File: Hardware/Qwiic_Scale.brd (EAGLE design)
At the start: 25.4 x 35.6 mm, 68 parts, among them J2 Qwiic Right Angle, J3 PTH, J4 Qwiic Right Angle, J6 Spring Terminal, U1 NAU7802

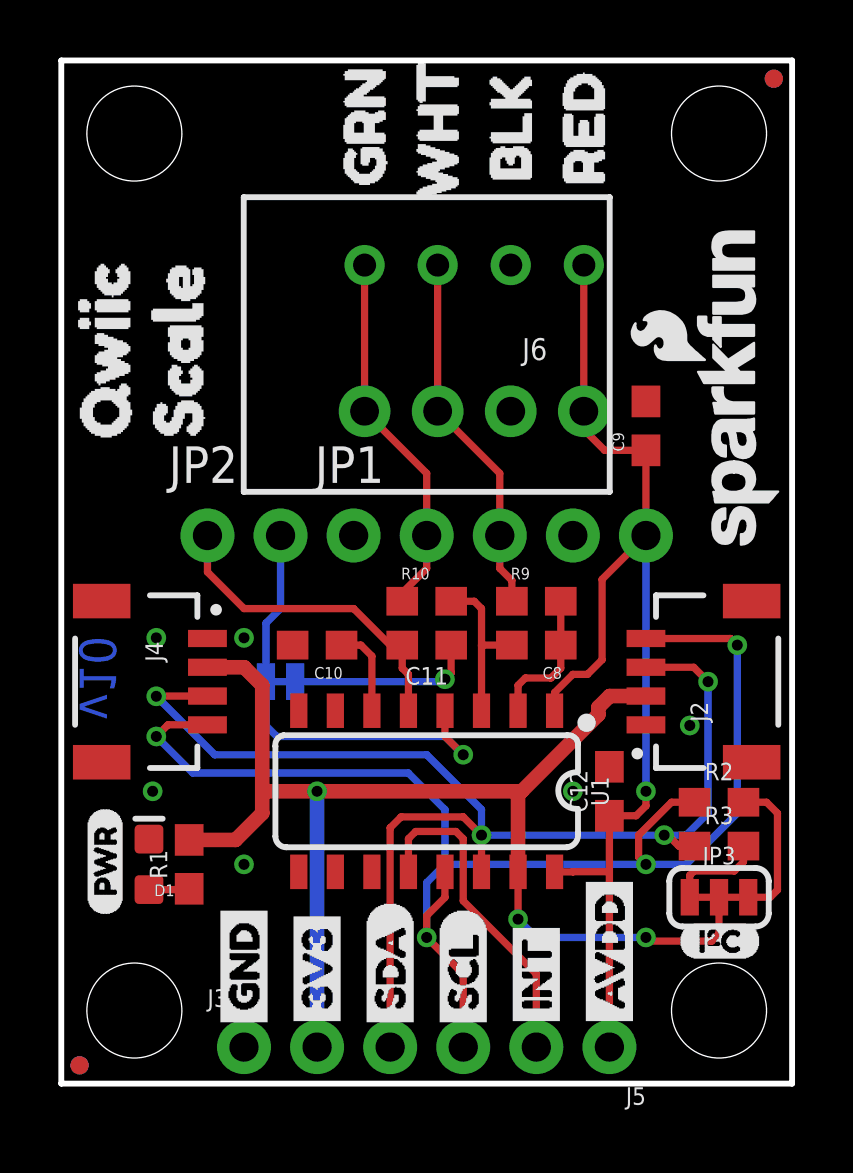
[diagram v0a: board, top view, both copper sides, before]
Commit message: Fixing FP on terminal. Adding ignore.
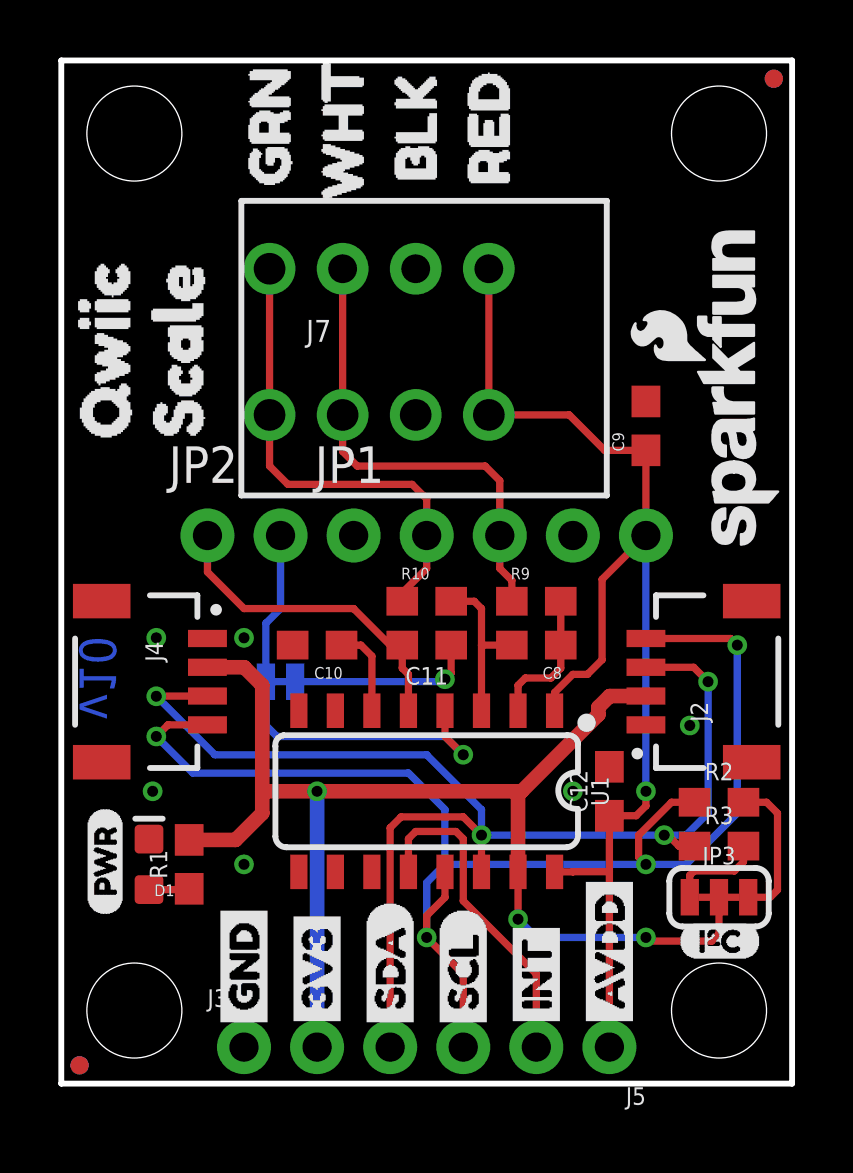
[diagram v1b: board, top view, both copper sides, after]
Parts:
- removed J6: Spring Terminal, SparkFun-Connectors:1X04_SPRING_TERMINAL
- added J7: Spring Terminal, SparkFun-Connectors:1X04_SPRING_TERMINAL
- moved U$41 3.30 mm to (14.9, 30.0)
- moved U$42 3.30 mm to (14.9, 30.4)
- moved U$40 3.30 mm to (7.24, 30.0)
- moved U$37 3.30 mm to (12.3, 29.0)
- moved U$38 3.30 mm to (12.3, 30.1)
- moved U$44 3.30 mm to (9.78, 29.5)
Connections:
- net A+: now also J7.4, J7.8; no longer J6.4, J6.8
- net A-: now also J7.3, J7.7; no longer J6.3, J6.7
- net GND: now also J7.2, J7.6; no longer J6.2, J6.6
- net VDDA: now also J7.1, J7.5; no longer J6.1, J6.5
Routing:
- net A-: track 12.8 -> 16.6 mm
- net A+: track 12.9 -> 16.7 mm
- net VDDA: track 39.6 -> 42.5 mm
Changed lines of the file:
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@@
 <attribute name="VALUE" x="20.32" y="3.302" size="0.6096" layer="27" font="vector" ratio="20" rot="R180"/>
-</element>
-<element name="J6" library="SparkFun-Connectors" package="1X04_SPRING_TERMINAL" value="Spring Terminal" x="18.161" y="25.908" smashed="yes" rot="R180">
-<attribute name="NAME" x="16.891" y="25.908" size="0.762" layer="25" rot="R180"/>
-<attribute name="SF_ID" value="PRT-08075" x="18.161" y="25.908" size="1.778" layer="27" font="vector" ratio="15" rot="R180" display="off"/>
-<attribute name="VALUE" x="16.891" y="27.178" size="0.762" layer="27" rot="R180"/>
 </element>
 <element name="U$12" library="buzzard_labels (62)" package="B#11" value="" x="7.62" y="15.24" smashed="yes" rot="MR90"/>
 <element name="U$13" library="buzzard_labels (62)" package="B#12" value="" x="5.08" y="15.24" smashed="yes" rot="MR90"/>
-<element name="U$37" library="buzzard_labels (64)" package="BLACK5" value="" x="15.621" y="28.956" smashed="yes" rot="MR90"/>
-<element name="U$38" library="buzzard_labels (64)" package="BLK1" value="" x="15.621" y="30.099" smashed="yes" rot="R90"/>
+<element name="U$37" library="buzzard_labels (64)" package="BLACK5" value="" x="12.319" y="28.956" smashed="yes" rot="MR90"/>
+<element name="U$38" library="buzzard_labels (64)" package="BLK1" value="" x="12.319" y="30.099" smashed="yes" rot="R90"/>
 <element name="U$39" library="buzzard_labels (64)" package="GREEN7" value="" x="10.668" y="28.321" smashed="yes" rot="MR90"/>
-<element name="U$40" library="buzzard_labels (64)" package="GRN3" value="" x="10.541" y="29.972" smashed="yes" rot="R90"/>
-<element name="U$41" library="buzzard_labels (64)" package="RED0" value="" x="18.161" y="29.972" smashed="yes" rot="R90"/>
-<element name="U$42" library="buzzard_labels (64)" package="RED4" value="" x="18.161" y="30.353" smashed="yes" rot="MR90"/>
+<element name="U$40" library="buzzard_labels (64)" package="GRN3" value="" x="7.239" y="29.972" smashed="yes" rot="R90"/>
+<element name="U$41" library="buzzard_labels (64)" package="RED0" value="" x="14.859" y="29.972" smashed="yes" rot="R90"/>
+<element name="U$42" library="buzzard_labels (64)" package="RED4" value="" x="14.859" y="30.353" smashed="yes" rot="MR90"/>
 <element name="U$43" library="buzzard_labels (64)" package="WHITE6" value="" x="13.081" y="28.067" smashed="yes" rot="MR90"/>
-<element name="U$44" library="buzzard_labels (64)" package="WHT2" value="" x="13.081" y="29.464" smashed="yes" rot="R90"/>
+<element name="U$44" library="buzzard_labels (64)" package="WHT2" value="" x="9.779" y="29.464" smashed="yes" rot="R90"/>
 <element name="U$34" library="buzzard_labels (65)" package="BLK#E#1" value="" x="17.78" y="11.938" smashed="yes" rot="MR90"/>
 <element name="U$35" library="buzzard_labels (65)" package="GRN#A#4" value="" x="12.7" y="11.43" smashed="yes" rot="MR90"/>
@@
 </element>
 <element name="U$19" library="Labels" package="I_SUPER2_C-()-03" value="" x="21.463" y="4.953" smashed="yes"/>
+<element name="J7" library="SparkFun-Connectors" package="1X04_SPRING_TERMINAL" value="Spring Terminal" x="7.239" y="25.781" smashed="yes">
+<attribute name="NAME" x="8.509" y="25.781" size="0.762" layer="25"/>
+<attribute name="SF_ID" value="PRT-08075" x="7.239" y="25.781" size="1.778" layer="27" font="vector" ratio="15" display="off"/>
+<attribute name="VALUE" x="8.509" y="24.511" size="0.762" layer="27"/>
+</element>
 </elements>
 <signals>
@@
 <contactref element="U1" pad="8"/>
 <contactref element="C10" pad="2"/>
-<contactref element="J6" pad="6"/>
-<contactref element="J6" pad="2"/>
 <via x="17.78" y="10.16" extent="1-16" drill="0.381"/>
 <via x="6.35" y="7.62" extent="1-16" drill="0.381"/>
@@
 <via x="21.844" y="12.446" extent="1-16" drill="0.381"/>
 <via x="6.35" y="15.494" extent="1-16" drill="0.381"/>
+<contactref element="J7" pad="2"/>
+<contactref element="J7" pad="6"/>
 </signal>
 <signal name="SCL">
@@
 <contactref element="JP1" pad="5"/>
 <contactref element="J5" pad="1"/>
-<contactref element="J6" pad="5"/>
-<contactref element="J6" pad="1"/>
 <via x="20.32" y="10.16" extent="1-16" drill="0.381"/>
 <wire x1="20.32" y1="10.16" x2="20.32" y2="19.05" width="0.254" layer="16"/>
 <wire x1="17.145" y1="7.36" x2="17.78" y2="7.36" width="0.254" layer="1"/>
-<wire x1="18.161" y1="23.368" x2="18.161" y2="28.448" width="0.254" layer="1"/>
 <wire x1="17.145" y1="12.96" x2="17.145" y2="13.589" width="0.254" layer="1"/>
 <wire x1="17.145" y1="13.589" x2="17.78" y2="14.224" width="0.254" layer="1"/>
@@
 <wire x1="20.32" y1="9.652" x2="20.32" y2="10.16" width="0.254" layer="1"/>
 <wire x1="20.32" y1="19.05" x2="20.32" y2="22.01" width="0.254" layer="1"/>
-<wire x1="20.32" y1="22.01" x2="18.884" y2="22.01" width="0.254" layer="1"/>
-<wire x1="18.884" y1="22.01" x2="18.161" y2="22.733" width="0.254" layer="1"/>
-<wire x1="18.161" y1="22.733" x2="18.161" y2="23.368" width="0.254" layer="1"/>
+<wire x1="18.884" y1="22.01" x2="20.32" y2="22.01" width="0.254" layer="1"/>
+<contactref element="J7" pad="5"/>
+<contactref element="J7" pad="1"/>
+<wire x1="14.859" y1="23.241" x2="17.653" y2="23.241" width="0.254" layer="1"/>
+<wire x1="17.653" y1="23.241" x2="18.884" y2="22.01" width="0.254" layer="1"/>
+<wire x1="14.859" y1="23.241" x2="14.859" y2="28.321" width="0.254" layer="1"/>
 </signal>
 <signal name="N$11">
@@
 <contactref element="R9" pad="1"/>
 <contactref element="JP1" pad="3"/>
-<contactref element="J6" pad="7"/>
-<contactref element="J6" pad="3"/>
-<wire x1="13.081" y1="23.368" x2="13.081" y2="28.448" width="0.254" layer="1"/>
-<wire x1="15.24" y1="19.05" x2="15.24" y2="21.209" width="0.254" layer="1"/>
-<wire x1="15.24" y1="21.209" x2="13.081" y2="23.368" width="0.254" layer="1"/>
 <wire x1="15.66" y1="16.764" x2="15.66" y2="17.487" width="0.254" layer="1"/>
 <wire x1="15.66" y1="17.487" x2="15.24" y2="17.907" width="0.254" layer="1"/>
 <wire x1="15.24" y1="17.907" x2="15.24" y2="19.05" width="0.254" layer="1"/>
+<contactref element="J7" pad="7"/>
+<contactref element="J7" pad="3"/>
+<wire x1="9.779" y1="28.321" x2="9.779" y2="23.241" width="0.254" layer="1"/>
+<wire x1="9.779" y1="23.241" x2="9.779" y2="21.971" width="0.254" layer="1"/>
+<wire x1="9.779" y1="21.971" x2="10.287" y2="21.463" width="0.254" layer="1"/>
+<wire x1="10.287" y1="21.463" x2="14.732" y2="21.463" width="0.254" layer="1"/>
+<wire x1="14.732" y1="21.463" x2="15.24" y2="20.955" width="0.254" layer="1"/>
+<wire x1="15.24" y1="20.955" x2="15.24" y2="19.05" width="0.254" layer="1"/>
 </signal>
 <signal name="A+">
 <contactref element="R10" pad="1"/>
 <contactref element="JP1" pad="2"/>
-<contactref element="J6" pad="4"/>
-<contactref element="J6" pad="8"/>
-<wire x1="10.541" y1="23.368" x2="10.541" y2="28.448" width="0.254" layer="1"/>
-<wire x1="12.7" y1="19.05" x2="12.7" y2="21.209" width="0.254" layer="1"/>
-<wire x1="12.7" y1="21.209" x2="10.541" y2="23.368" width="0.254" layer="1"/>
 <wire x1="11.85" y1="16.764" x2="11.85" y2="17.057" width="0.254" layer="1"/>
 <wire x1="11.85" y1="17.057" x2="12.7" y2="17.907" width="0.254" layer="1"/>
 <wire x1="12.7" y1="17.907" x2="12.7" y2="19.05" width="0.254" layer="1"/>
+<contactref element="J7" pad="4"/>
+<contactref element="J7" pad="8"/>
+<wire x1="12.7" y1="19.05" x2="12.7" y2="20.32" width="0.254" layer="1"/>
+<wire x1="12.7" y1="20.32" x2="12.192" y2="20.828" width="0.254" layer="1"/>
+<wire x1="12.192" y1="20.828" x2="7.874" y2="20.828" width="0.254" layer="1"/>
+<wire x1="7.874" y1="20.828" x2="7.239" y2="21.463" width="0.254" layer="1"/>
+<wire x1="7.239" y1="21.463" x2="7.239" y2="23.241" width="0.254" layer="1"/>
+<wire x1="7.239" y1="23.241" x2="7.239" y2="28.321" width="0.254" layer="1"/>
 </signal>
 <signal name="N$1">
